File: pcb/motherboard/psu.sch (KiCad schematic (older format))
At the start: 22 parts, among them J11 Standoff, J12 Standoff, J9 AUX PWR, U3 ADP2302, U4 ADP2302

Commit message: Changed crystal location for PCM2704
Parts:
- added J16: Standoff, Conn-Header:HDR-M-1x01, symbol HEADER-1x01
- U3: value ADP2302 -> ADP2302ARDZ-5.0
- U4: value ADP2302 -> ADP2303ARDZ-3.3; symbol ADP2302 -> ADP2303
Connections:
- no-connect marks 0 -> 5
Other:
- moved on the sheet: J11, J12
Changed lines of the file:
@@
 P 6200 3000
 F 0 "U3" H 5850 3450 60  0000 L BNB
-F 1 "ADP2302" H 5850 2550 40  0000 L TNN
+F 1 "ADP2302ARDZ-5.0" H 5850 2550 40  0000 L TNN
 F 2 "SMT-SOIC:8-EP" H 5850 2450 40  0001 L CNN
 F 3 "" H 5450 2500 60  0000 C CNN
@@
 $EndComp
 $Comp
-L GND #PWR019
+L GND #PWR020
 U 1 1 54FECCC2
 P 7950 3100
-F 0 "#PWR019" H 7950 3150 30  0001 C CNN
+F 0 "#PWR020" H 7950 3150 30  0001 C CNN
 F 1 "GND" H 7950 2975 30  0001 C CNN
 F 2 "" H 7950 3100 60  0000 C CNN
@@
 $EndComp
 $Comp
-L GND #PWR020
+L GND #PWR021
 U 1 1 54FECEBA
 P 9050 3100
-F 0 "#PWR020" H 9050 3150 30  0001 C CNN
+F 0 "#PWR021" H 9050 3150 30  0001 C CNN
 F 1 "GND" H 9050 2975 30  0001 C CNN
 F 2 "" H 9050 3100 60  0000 C CNN
@@
 $EndComp
 $Comp
-L GND #PWR021
+L GND #PWR022
 U 1 1 54FECED6
 P 9500 3300
-F 0 "#PWR021" H 9500 3350 30  0001 C CNN
+F 0 "#PWR022" H 9500 3350 30  0001 C CNN
 F 1 "GND" H 9500 3175 30  0001 C CNN
 F 2 "" H 9500 3300 60  0000 C CNN
@@
 $EndComp
 $Comp
-L SUP_+5V #PWR022
+L SUP_+5V #PWR023
 U 1 1 54FED337
 P 9500 2550
-F 0 "#PWR022" H 9500 2775 30  0001 C CNN
+F 0 "#PWR023" H 9500 2775 30  0001 C CNN
 F 1 "SUP_+5V" V 9425 2550 30  0001 C CNN
 F 2 "" H 9400 2675 60  0001 C CNN
@@
 $EndComp
 $Comp
-L GND #PWR023
+L GND #PWR024
 U 1 1 54FED6CA
 P 5600 3500
-F 0 "#PWR023" H 5600 3550 30  0001 C CNN
+F 0 "#PWR024" H 5600 3550 30  0001 C CNN
 F 1 "GND" H 5600 3375 30  0001 C CNN
 F 2 "" H 5600 3500 60  0000 C CNN
@@
 $EndComp
 $Comp
-L GND #PWR024
+L GND #PWR025
 U 1 1 54FED9CB
 P 5050 3100
-F 0 "#PWR024" H 5050 3150 30  0001 C CNN
+F 0 "#PWR025" H 5050 3150 30  0001 C CNN
 F 1 "GND" H 5050 2975 30  0001 C CNN
 F 2 "" H 5050 3100 60  0000 C CNN
@@
 $EndComp
 $Comp
-L ADP2302 U4
+L ADP2303 U4
 U 1 1 54FEE1F8
 P 6200 5400
 F 0 "U4" H 5850 5850 60  0000 L BNB
-F 1 "ADP2302" H 5850 4950 40  0000 L TNN
+F 1 "ADP2303ARDZ-3.3" H 5850 4950 40  0000 L TNN
 F 2 "SMT-SOIC:8-EP" H 5850 4850 40  0001 L CNN
 F 3 "" H 5450 4900 60  0000 C CNN
@@
 $EndComp
 $Comp
-L GND #PWR025
+L GND #PWR026
 U 1 1 54FEE219
 P 7950 5500
-F 0 "#PWR025" H 7950 5550 30  0001 C CNN
+F 0 "#PWR026" H 7950 5550 30  0001 C CNN
 F 1 "GND" H 7950 5375 30  0001 C CNN
 F 2 "" H 7950 5500 60  0000 C CNN
@@
 $EndComp
 $Comp
-L GND #PWR026
+L GND #PWR027
 U 1 1 54FEE235
 P 9050 5500
-F 0 "#PWR026" H 9050 5550 30  0001 C CNN
+F 0 "#PWR027" H 9050 5550 30  0001 C CNN
 F 1 "GND" H 9050 5375 30  0001 C CNN
 F 2 "" H 9050 5500 60  0000 C CNN
@@
 $EndComp
 $Comp
-L GND #PWR027
+L GND #PWR028
 U 1 1 54FEE23B
 P 9500 5700
-F 0 "#PWR027" H 9500 5750 30  0001 C CNN
+F 0 "#PWR028" H 9500 5750 30  0001 C CNN
 F 1 "GND" H 9500 5575 30  0001 C CNN
 F 2 "" H 9500 5700 60  0000 C CNN
@@
 $EndComp
 $Comp
-L GND #PWR028
+L GND #PWR029
 U 1 1 54FEE24A
 P 5600 5900
-F 0 "#PWR028" H 5600 5950 30  0001 C CNN
+F 0 "#PWR029" H 5600 5950 30  0001 C CNN
 F 1 "GND" H 5600 5775 30  0001 C CNN
 F 2 "" H 5600 5900 60  0000 C CNN
@@
 $EndComp
 $Comp
-L GND #PWR029
+L GND #PWR030
 U 1 1 54FEE260
 P 5050 5500
-F 0 "#PWR029" H 5050 5550 30  0001 C CNN
+F 0 "#PWR030" H 5050 5550 30  0001 C CNN
 F 1 "GND" H 5050 5375 30  0001 C CNN
 F 2 "" H 5050 5500 60  0000 C CNN
@@
 $EndComp
 $Comp
-L SUP_+3V3 #PWR030
+L SUP_+3V3 #PWR031
 U 1 1 54FEE339
 P 9500 4950
-F 0 "#PWR030" H 9500 5175 30  0001 C CNN
+F 0 "#PWR031" H 9500 5175 30  0001 C CNN
 F 1 "SUP_+3V3" V 9425 4950 30  0001 C CNN
 F 2 "" H 9400 5075 60  0001 C CNN
@@
 $EndComp
 $Comp
-L GND #PWR031
+L GND #PWR032
 U 1 1 54FEF30E
 P 2450 3200
-F 0 "#PWR031" H 2450 3250 30  0001 C CNN
+F 0 "#PWR032" H 2450 3250 30  0001 C CNN
 F 1 "GND" H 2450 3075 30  0001 C CNN
 F 2 "" H 2450 3200 60  0000 C CNN
@@
 $EndComp
 $Comp
-L GND #PWR032
+L GND #PWR033
 U 1 1 54FEF5ED
 P 3150 5250
-F 0 "#PWR032" H 3150 5300 30  0001 C CNN
+F 0 "#PWR033" H 3150 5300 30  0001 C CNN
 F 1 "GND" H 3150 5125 30  0001 C CNN
 F 2 "" H 3150 5250 60  0000 C CNN
@@
 VIN
 $Comp
-L SUP_+9V #PWR033
+L SUP_+9V #PWR034
 U 1 1 54FF0A98
 P 2350 4700
-F 0 "#PWR033" H 2350 4925 30  0001 C CNN
+F 0 "#PWR034" H 2350 4925 30  0001 C CNN
 F 1 "SUP_+9V" V 2275 4700 30  0001 C CNN
 F 2 "" H 2250 4825 60  0001 C CNN
@@
 $EndComp
 $Comp
-L +3V3 #PWR034
+L +3V3 #PWR035
 U 1 1 54FF1E66
 P 2100 4700
-F 0 "#PWR034" H 2100 4925 30  0001 C CNN
+F 0 "#PWR035" H 2100 4925 30  0001 C CNN
 F 1 "+3V3" V 2025 4700 30  0001 C CNN
 F 2 "" H 2100 4700 60  0000 C CNN
@@
 	5050 5400 5050 5500
 Wire Wire Line
-	2750 3000 2900 3000
-Wire Wire Line
-	2900 3000 2900 3200
-Wire Wire Line
 	2550 3000 2450 3000
 Wire Wire Line
@@
 	5050 2550 5050 2800
 $Comp
-L +9V #PWR035
+L +9V #PWR036
 U 1 1 550419F4
 P 5050 4950
-F 0 "#PWR035" H 5050 5175 30  0001 C CNN
+F 0 "#PWR036" H 5050 5175 30  0001 C CNN
 F 1 "+9V" V 4975 4950 30  0001 C CNN
 F 2 "" H 5050 4950 60  0000 C CNN
@@
 	5050 5100 5750 5100
 $Comp
-L +9V #PWR036
+L +9V #PWR037
 U 1 1 55043508
 P 5050 2550
-F 0 "#PWR036" H 5050 2775 30  0001 C CNN
+F 0 "#PWR037" H 5050 2775 30  0001 C CNN
 F 1 "+9V" V 4975 2550 30  0001 C CNN
 F 2 "" H 5050 2550 60  0000 C CNN
@@
 Connection ~ 5600 2700
 $Comp
-L +9V #PWR037
+L +9V #PWR038
 U 1 1 55044104
 P 3000 4700
-F 0 "#PWR037" H 3000 4925 30  0001 C CNN
+F 0 "#PWR038" H 3000 4925 30  0001 C CNN
 F 1 "+9V" V 2925 4700 30  0001 C CNN
 F 2 "" H 3000 4700 60  0000 C CNN
@@
 	3000 5200 2850 5200
 $Comp
-L GND #PWR038
+L GND #PWR039
 U 1 1 55045860
 P 2100 5250
-F 0 "#PWR038" H 2100 5300 30  0001 C CNN
+F 0 "#PWR039" H 2100 5300 30  0001 C CNN
 F 1 "GND" H 2100 5125 30  0001 C CNN
 F 2 "" H 2100 5250 60  0000 C CNN
@@
 $EndComp
 $Comp
-L SUP_GNDPWR #PWR039
-U 1 1 5504689F
-P 2900 3200
-F 0 "#PWR039" H 2900 3250 30  0001 C CNN
-F 1 "SUP_GNDPWR" H 2900 3075 30  0001 C CNN
-F 2 "" H 2900 3150 60  0000 C CNN
-F 3 "" H 2900 3150 60  0000 C CNN
-	1    2900 3200
-	1    0    0    -1
-$EndComp
-$Comp
 L HEADER-1x01 J11
 U 1 1 5505C11C
-P 2650 1800
-F 0 "J11" H 2600 1900 60  0000 L BNB
-F 1 "Standoff" V 2800 1800 40  0001 C CNN
-F 2 "Conn-Header:HDR-M-1x01" H 2500 1775 60  0001 C CNN
-F 3 "" H 2600 1875 60  0001 C CNN
-	1    2650 1800
+P 2650 1350
+F 0 "J11" H 2600 1450 60  0000 L BNB
+F 1 "Standoff" V 2800 1350 40  0001 C CNN
+F 2 "Conn-Header:HDR-M-1x01" H 2500 1325 60  0001 C CNN
+F 3 "" H 2600 1425 60  0001 C CNN
+	1    2650 1350
 	1    0    0    -1
 $EndComp
@@
 L HEADER-1x01 J12
 U 1 1 5505C18A
-P 2650 2100
-F 0 "J12" H 2600 2200 60  0000 L BNB
-F 1 "Standoff" V 2800 2100 40  0001 C CNN
-F 2 "Conn-Header:HDR-M-1x01" H 2500 2075 60  0001 C CNN
-F 3 "" H 2600 2175 60  0001 C CNN
-	1    2650 2100
+P 2650 1650
+F 0 "J12" H 2600 1750 60  0000 L BNB
+F 1 "Standoff" V 2800 1650 40  0001 C CNN
+F 2 "Conn-Header:HDR-M-1x01" H 2500 1625 60  0001 C CNN
+F 3 "" H 2600 1725 60  0001 C CNN
+	1    2650 1650
 	1    0    0    -1
 $EndComp
@@
 Text Notes 2050 4350 0    100  ~ 0
 BATTERY MODULE
+$Comp
+L HEADER-1x01 J16
+U 1 1 550BA738
+P 2650 1950
+F 0 "J16" H 2600 2050 60  0000 L BNB
+F 1 "Standoff" V 2800 1950 40  0001 C CNN
+F 2 "Conn-Header:HDR-M-1x01" H 2500 1925 60  0001 C CNN
+F 3 "" H 2600 2025 60  0001 C CNN
+	1    2650 1950
+	1    0    0    -1
+$EndComp
+NoConn ~ 5750 5400
+NoConn ~ 5750 3000
+NoConn ~ 2500 1950
+NoConn ~ 2500 1650
+NoConn ~ 2500 1350
+$Comp
+L SUP_GNDPWR #PWR040
+U 1 1 550DC48F
+P 2900 3200
+F 0 "#PWR040" H 2900 3250 30  0001 C CNN
+F 1 "SUP_GNDPWR" H 2900 3075 30  0001 C CNN
+F 2 "" H 2900 3150 60  0000 C CNN
+F 3 "" H 2900 3150 60  0000 C CNN
+	1    2900 3200
+	1    0    0    -1
+$EndComp
+Wire Wire Line
+	2750 3000 2900 3000
+Wire Wire Line
+	2900 3000 2900 3200
 $EndSCHEMATC

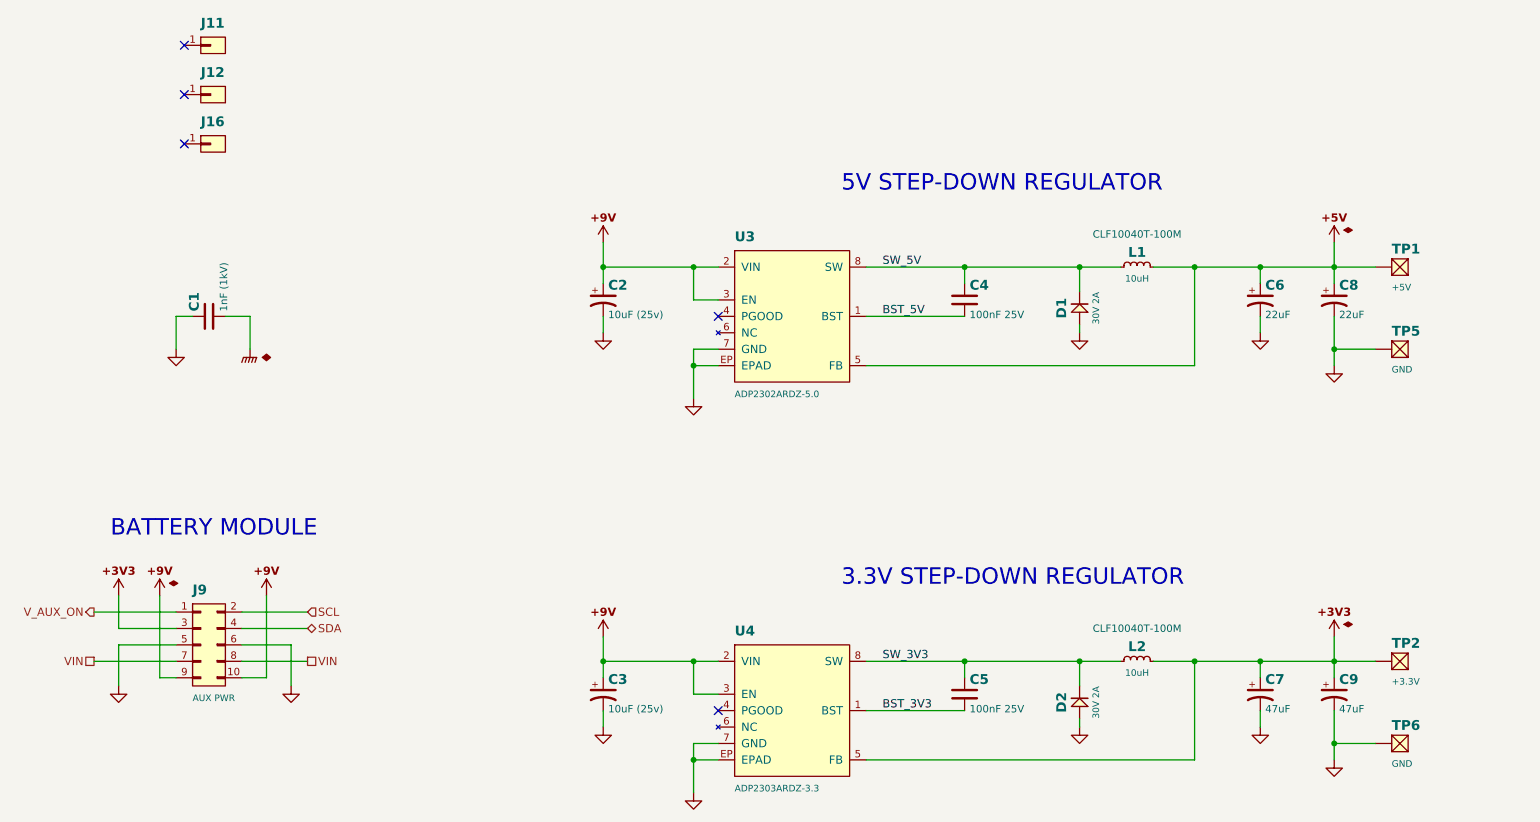
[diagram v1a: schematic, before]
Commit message: Tidy up motherboard schematic
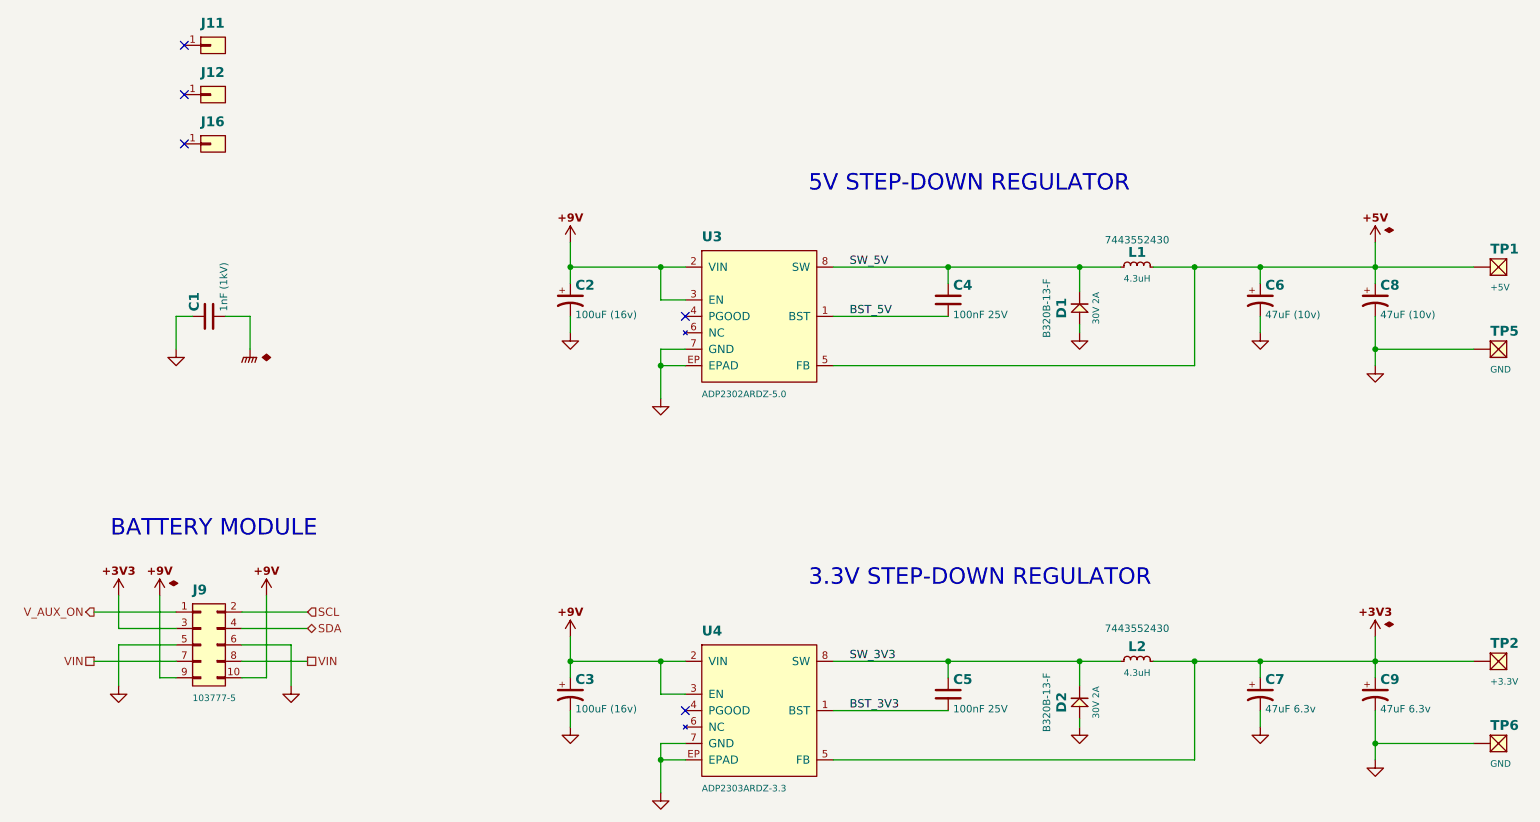
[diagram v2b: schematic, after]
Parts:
- C1, C4, C5: Family (none) -> Passive
- C2, C3: value 10uF (25v) -> 100uF (16v); Family (none) -> Passive; MFG (none) -> Taiyo Yuden; Part (none) -> EMK325ABJ107MM-T; Part# - -> (none)
- C6, C8: value 22uF -> 47uF (10v); Family (none) -> Passive; MFG (none) -> Taiyo Yuden; Part (none) -> LMK316BJ476ML-T; Part# - -> (none)
- C7: value 47uF -> 47uF 6.3v; Family (none) -> Passive; MFG (none) -> Murata; Part (none) -> GRM31CR60J476ME19K; Part# - -> (none)
- C9: value 47uF -> 47uF 6.3v; Family (none) -> Passive; MFG (none) -> Murata; Part# - -> GRM31CR60J476ME19K
- D1: Family (none) -> Passive; MFG (none) -> Diodes Inc; PART - -> B320B-13-F
- D2: Family (none) -> Passive; MFG (none) -> Diodes Inc; PART - -> (none); Part (none) -> B320B-13-F
- J11, J12, J16: value Standoff -> 103741-1; Family (none) -> Connector; MFG (none) -> TE Connectivity
- J9: value AUX PWR -> 103777-5; Family (none) -> Connector; MFG (none) -> TE Connectivity
- L1: value 10uH -> 4.3uH; Family (none) -> Passive; PART CLF10040T-100M -> 7443552430
- L2: value 10uH -> 4.3uH; Family (none) -> Passive; MFG (none) -> Wurth; PART CLF10040T-100M -> 7443552430
- TP1, TP2, TP5, TP6: Family (none) -> Virtual
- U3, U4: Family (none) -> IC; MFG (none) -> Analog Devices
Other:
- moved on the sheet: C2, C3, C4, C5, C8, C9, TP1, TP2, TP5, TP6, U3, U4
